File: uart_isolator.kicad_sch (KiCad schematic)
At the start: 15 parts, among them J1 Conn_01x02_Pin, J2 Conn_01x02_Pin, J3 Conn_01x02_Pin, J4 Conn_01x02_Pin, J5 Conn_01x02_Pin, J6 Conn_01x02_Pin, J7 Conn_01x04_Pin, Q1 BSS123, Q2 BSS123, U1 TLP175A

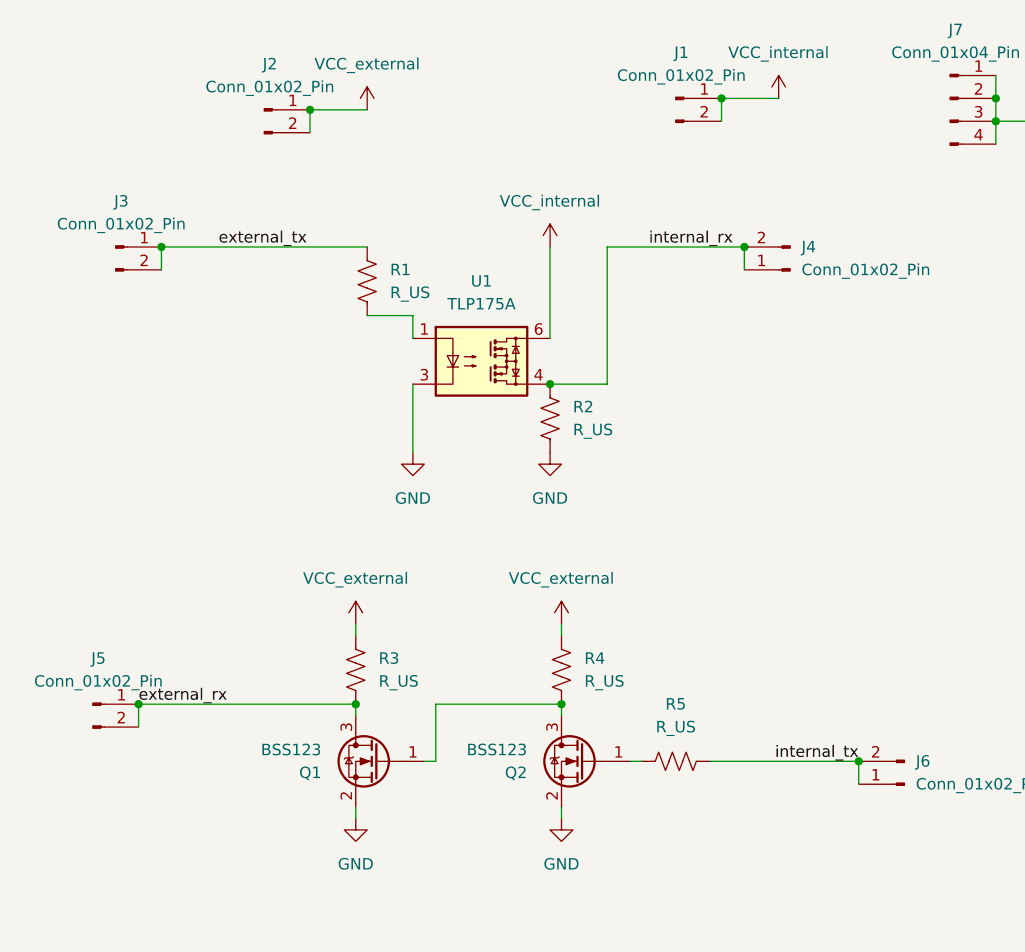
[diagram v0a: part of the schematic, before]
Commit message: Change to using voltage buffer
 - Silkmask updates to clarify labels
 - Using voltage buffer to isolate TX_in from RX_out
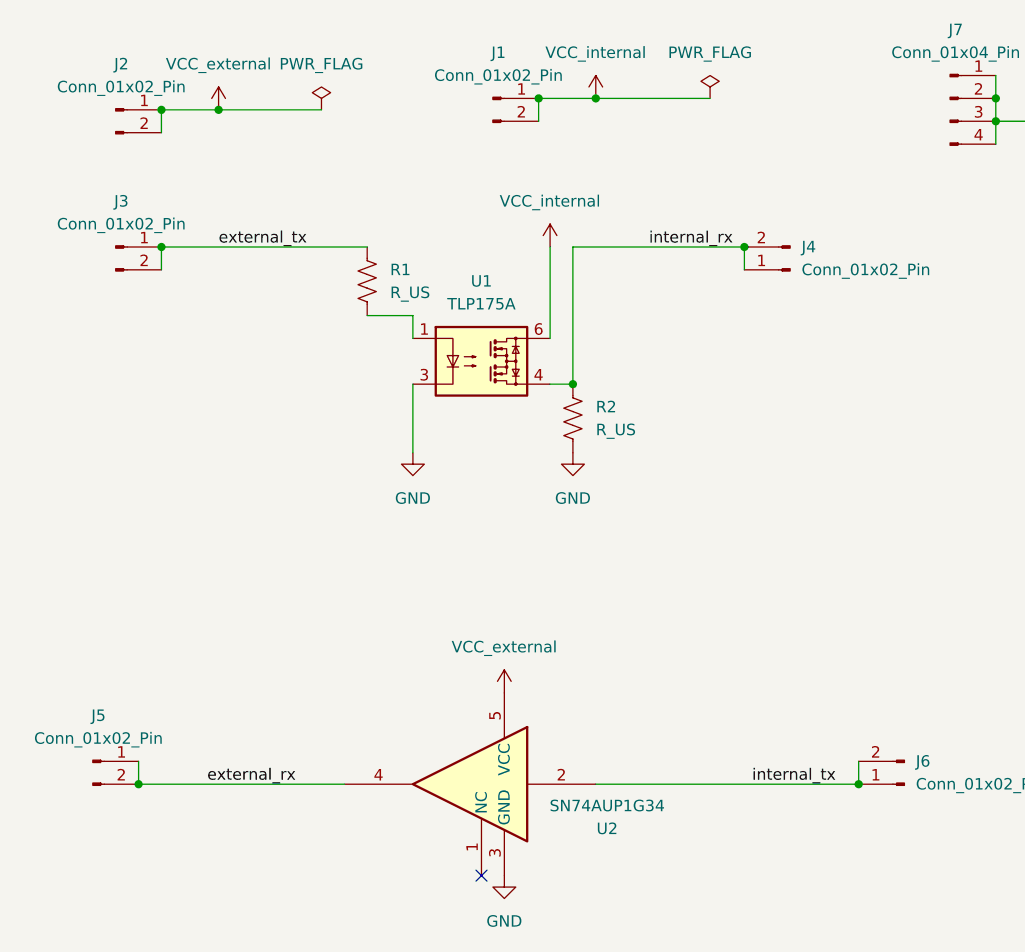
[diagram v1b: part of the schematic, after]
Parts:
- removed Q1, Q2: BSS123, Package_TO_SOT_SMD:SOT-23, symbol Transistor_FET:BSS123
- removed R3, R4, R5: R_US, Resistor_SMD:R_0603_1608Metric_Pad0.98x0.95mm_HandSolder, symbol Device:R_US
- added U2: SN74AUP1G34, Package_TO_SOT_SMD:SOT-23-5_HandSoldering, symbol 74xGxx:74AUP1G34
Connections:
- net GND: now also U2.3 (GND)
- net VCC_external: now also U2.5 (VCC)
- net external_rx: now also U2.4
- net internal_tx: now also U2.2
- no-connect marks 0 -> 1
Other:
- moved on the sheet: J1, J2, J5, R2

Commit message: Rev A
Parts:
- added C1, C2: 100n, Capacitor_SMD:C_0603_1608Metric_Pad1.08x0.95mm_HandSolder, symbol Device:C
- added C3, C4: 47p, Capacitor_SMD:C_0603_1608Metric_Pad1.08x0.95mm_HandSolder, symbol Device:C
- added C5, C6: 10u, Capacitor_SMD:C_0603_1608Metric_Pad1.08x0.95mm_HandSolder, symbol Device:C
- added D1, D2, D3: LED, LED_SMD:LED_0603_1608Metric_Pad1.05x0.95mm_HandSolder, symbol Device:LED
- added H1, H2, H3: MountingHole_Pad, MountingHole:MountingHole_2.2mm_M2_Pad_Via, symbol Mechanical:MountingHole_Pad
- added J10, J11, J13, J14, J15, J16, J8, J9: Conn_01x02_Pin, Connector_PinHeader_2.54mm:PinHeader_1x02_P2.54mm_Vertical, symbol Connector:Conn_01x02_Pin
- added J12: USB_C_Receptacle_USB2.0, Marcano:USB4105-GF-A, symbol Marcano_Connector:USB_C_Receptacle_USB2.0
- added R3, R4: 27, Resistor_SMD:R_0603_1608Metric_Pad0.98x0.95mm_HandSolder, symbol Device:R_US
- added R5, R6: 5.1k, Resistor_SMD:R_0603_1608Metric_Pad0.98x0.95mm_HandSolder, symbol Device:R_US
- added R7, R8, R9: 1k, Resistor_SMD:R_0603_1608Metric_Pad0.98x0.95mm_HandSolder, symbol Device:R_US
- added U3: FT230XS, Package_SO:SSOP-16_3.9x4.9mm_P0.635mm, symbol Interface_USB:FT230XS
- added U4: TLV74033PDBVR, Package_TO_SOT_SMD:SOT-23-5_HandSoldering, symbol Marcano_Voltage_Regulator:TLV74033PDBVR
- R1: value R_US -> 1k; Digikey Product Number (none) -> RMCF0603FT1K00TR-ND; Manufacturer Product Number (none) -> RMCF0603FT1K00
- R2: value R_US -> 95.3k; Digikey Product Number (none) -> 13-AC0603FR-0795K3LCT-ND; Manufacturer Product Number (none) -> AC0603FR-0795K3L
- U1: Digikey Product Number (none) -> TLP175A(TPLECT-ND; Manufacturer Product Number (none) -> TLP175A(TPL,E
- U2: Digikey Product Number (none) -> 296-19080-1-ND; Manufacturer Product Number (none) -> SN74AUP1G34DBVR
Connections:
- net GND: now also C1.2, C2.2, C3.2, C4.2, C5.2, C6.2, H1.1, H2.1, H3.1, J12.A1/B12 (GND), J12.A12/B1 (GND), J12.S1 (SHIELD), R5.2, R6.2, R7.2, U3.13 (GND), U3.5 (GND), U4.2 (GND)
- net VCC_external: now also C1.1, C2.1, C6.1, D1.2 (A), D2.2 (A), D3.2 (A), U3.11 (~{RESET}), U3.12 (VCC), U3.3 (VCCIO), U4.5 (3.3V_OUT)
- net external_rx: now also J9.2 (Pin_2)
- net external_tx: now also J8.2 (Pin_2)
- new net: J12.A5 (CC1), R5.1
- new net: D1.1 (K), R7.1
- new net: D2.1 (K), J14.1 (Pin_1), J14.2 (Pin_2), R8.1
- new net: D3.1 (K), J15.1 (Pin_1), J15.2 (Pin_2), R9.1
- new net: J9.1 (Pin_1), U3.4 (RXD)
- new net: R3.2, U3.9 (USBDM)
- new net: J8.1 (Pin_1), U3.1 (TXD)
- new net: J12.B5 (CC2), R6.1
- new net: J11.1 (Pin_1), J11.2 (Pin_2), U3.6 (~{CTS})
- new net: R9.2, U3.7 (CBUS2)
- new net: J13.1 (Pin_1), J13.2 (Pin_2), U3.15 (CBUS0)
- new net: J16.1 (Pin_1), J16.2 (Pin_2), U3.16 (CBUS3)
- new net: J10.1 (Pin_1), J10.2 (Pin_2), U3.2 (~{RTS})
- new net: R4.2, U3.8 (USBDP)
- new net: R8.2, U3.14 (CBUS1)
- new net USBDM: C4.1, J12.A7 (D-), J12.B7 (D-), R3.1
- new net USBDP: C3.1, J12.A6 (D+), J12.B6 (D+), R4.1
- new net VBUS_5V: C5.1, J12.A4/B9 (VBUS), J12.A9/B4 (VBUS), U4.1 (IN), U4.3 (EN)
- no-connect marks 1 -> 4
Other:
- note added: "Apparently the 47p caps on the USB data lines aren't mandatory-- they just seem to help with noise."
- note added: "Assume UART freq of 115200 baud Internal voltage domain is at 3.3V max. 6pF capacitance at pins. Assume fall time must be less than 1/3 of 1/115200 fall_time < 1/3 * 1/115200 fall_time = 5 * RC 5RC < 1 / (3 * 115200) R < 1/ (3 * 115200 * C * 5) R < 1/115200 * 1/90 * 10^12 R < 96450 96450 ohm @ 3.3V, that's 113 microwatts dissipated"
- note added: "External 5V and 3.3V domain Powered from USB"
- note added: "USB 3.3V LED indicator"
- company: (none) -> UC San Diego
- title: (none) -> UART Isolator
- moved on the sheet: J1, J2, J3, J4, J5, J6, J7, R1, R2, U1, U2
